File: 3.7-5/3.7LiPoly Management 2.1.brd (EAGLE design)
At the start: 25 x 55 mm, 32 parts, among them J1 DX4R005HJ5R2000, J2 S2B-PH-SM4-TB(LF)(SN), T1 MMUN2133LT1G, U1 TPS61090RSAR, U2 MCP73871T-2CCI/ML

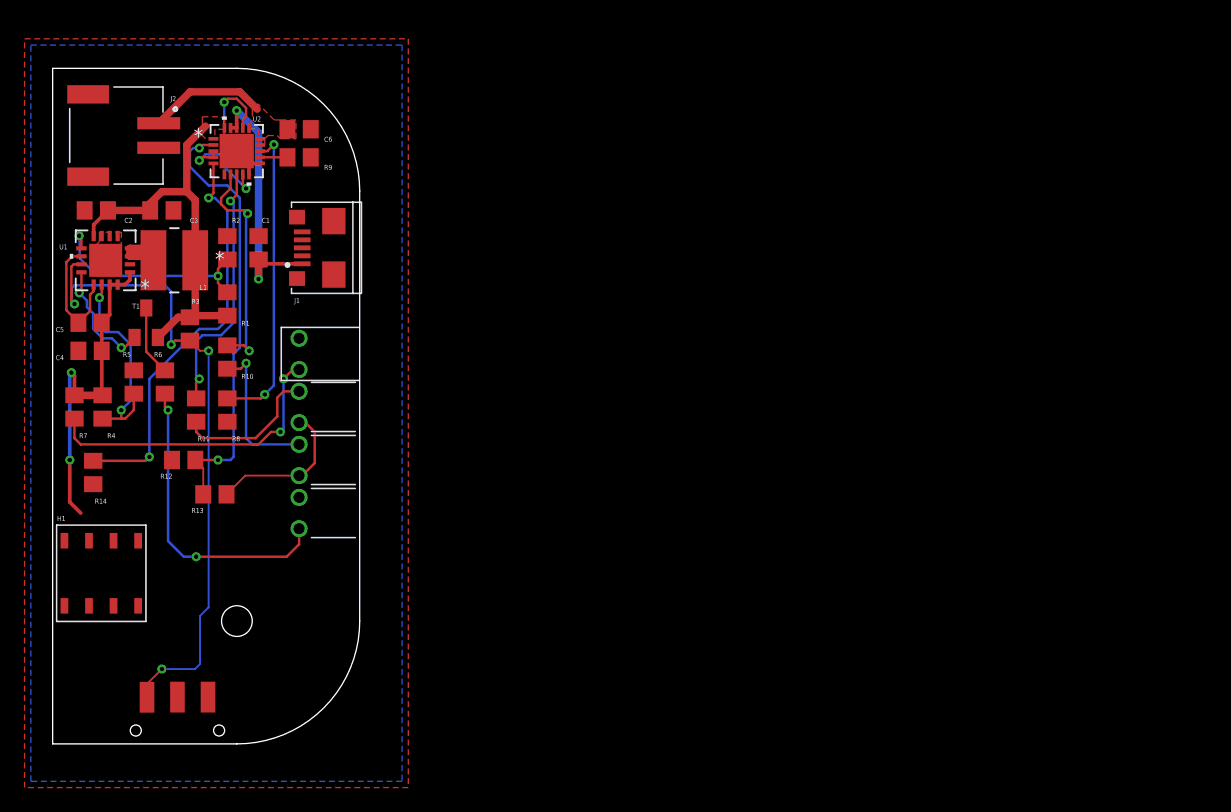
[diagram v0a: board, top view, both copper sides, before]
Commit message: Update
Moved shoulder buttons to LiPoly Management and extended LiPoly Management's dimensions. After looking at the boards in Fusion 360, I decided it would be better to have the shoulder buttons lower, rather than up high on RPi Zero Breakout. Rereouted LiPoly due to this.
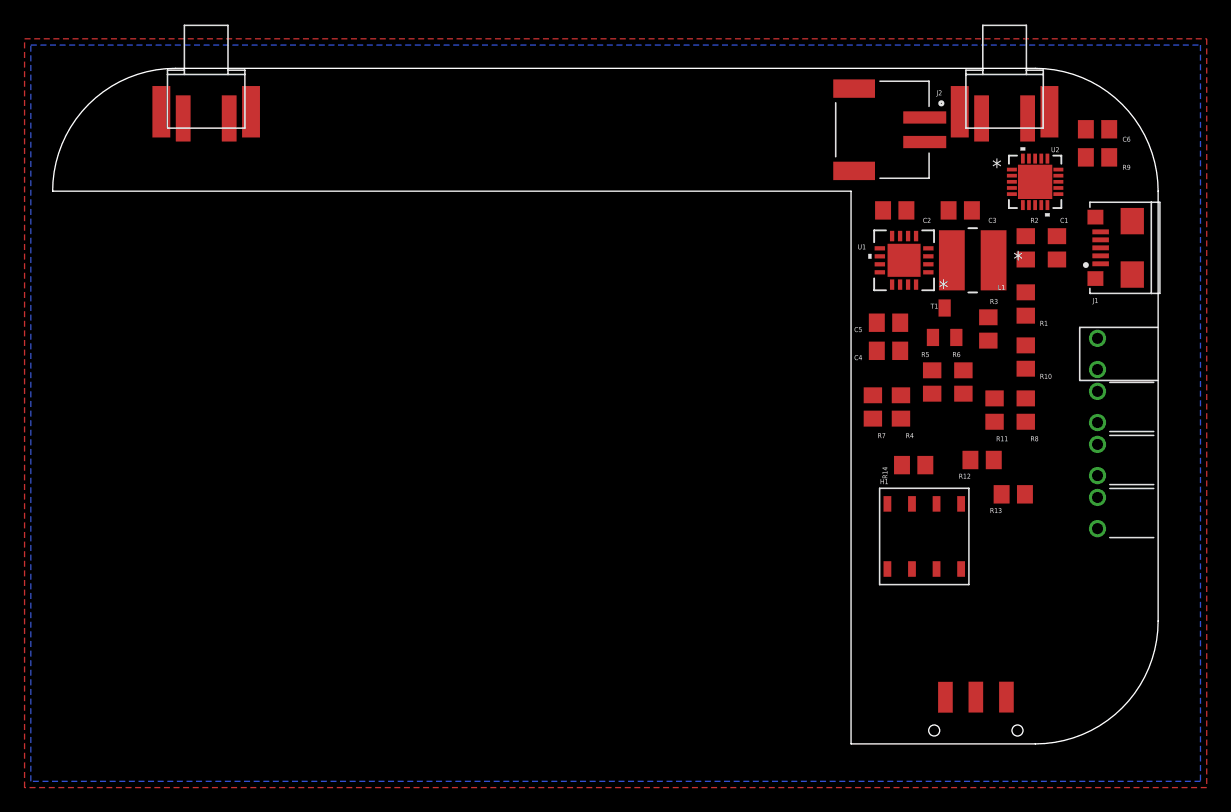
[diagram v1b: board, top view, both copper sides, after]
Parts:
- added U$1, U$3: SPST_TACTILE_SWITCHRIGHTANGLEBENT, switches:SPST_TACTILESWITCH_TL3360CF185Q_BENTFRAME
- moved H1 67.1 mm to (71.4, 17.0)
- moved R14 66.8 mm to (70.1, 22.7), turned to 0 degrees
- moved U2 65.0 mm to (80.0, 45.8)
- moved C1 65.0 mm to (81.8, 40.4)
- moved C2 65.0 mm to (68.6, 43.4)
- moved C3 65.0 mm to (73.9, 43.4)
- moved C4 65.0 mm to (68.0, 32.0)
- moved C5 65.0 mm to (68.0, 34.3)
- moved C6 65.0 mm to (85.1, 50.0)
- moved CHARGE 65.0 mm to (85.1, 27.4)
- moved DONE 65.0 mm to (85.1, 23.1)
- moved J1 65.0 mm to (85.3, 40.4)
- moved L1 65.0 mm to (74.9, 39.4)
- moved LBO 65.0 mm to (85.1, 18.8)
- moved POWERON 65.0 mm to (85.1, 31.8)
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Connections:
- new net N$10: H1.P4, U$3.P$1
- new net N$15: H1.P3, U$1.P$1
- net GND: now also U$1.P$2, U$3.P$2
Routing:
- net N$2: track 53.6 -> 0.00 mm, vias 4 -> 0
- net N$14: track 36.1 -> 0.00 mm, vias 2 -> 0
- net VBAT: track 33.6 -> 0.00 mm
- net N$13: track 33.2 -> 0.00 mm, vias 2 -> 0
- net VOUT: track 27.8 -> 0.00 mm, vias 2 -> 0
- net N$4: track 25.2 -> 0.00 mm, vias 2 -> 0
- net N$7: track 25.0 -> 0.00 mm, vias 2 -> 0
- net N$6: track 25.0 -> 0.00 mm, vias 2 -> 0
- net VBUS: track 22.2 -> 0.00 mm, vias 2 -> 0
- net N$11: track 20.9 -> 0.00 mm, vias 2 -> 0
- net N$12: track 18.5 -> 0.00 mm, vias 2 -> 0
- net N$1: track 18.1 -> 0.00 mm, vias 2 -> 0
- net FB: track 17.1 -> 0.00 mm, vias 2 -> 0
- net CTRL: track 16.9 -> 0.00 mm, vias 3 -> 0
- net GND: track 13.6 -> 0.00 mm
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- removed copper zone on layer 1, net VBAT
- removed copper zone on layer 1, net VLIPO
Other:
- board size 25 x 55 mm -> 90 x 55 mm
